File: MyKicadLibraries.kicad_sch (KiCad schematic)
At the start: 34 parts, among them J1 Conn_01x08, J10 RCJ-22, J11 DIN-5, J12 Mini-DIN-6, J13 USB_A, J2 Conn_01x08, J3 POGO Pins, J4 c8-inlet, J5 FTDI, J6 Micro_SD_Card, J7 Conn_01x04, J8 Conn_02x04_Counter_Clockwise, J9 Conn_01x04, SW1 Schurter Switch, U1 radio-receiver, U10 rdm-6300, U11 magnetic-charger, U12 adafruit-MAX98357, U13 TTL, U14 lxb18, U15 esp32-wemos-d1-mini, U16 TCRT5000, U17 opb607a, U2 TP4056, U3 LilygoSIMT7000G, U4 esp-01m, U5 relais_module, U6 ESP-01, U7 dcdc, U8 mems-mic, U9 ESP-12E

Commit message: Add OPB607a breakout
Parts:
- added J14, J15: Conn_01x02, Connector_PinHeader_2.54mm:PinHeader_1x02_P2.54mm_Vertical, symbol Connector_Generic:Conn_01x02
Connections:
- net at U17.1: now also J15.2 (Pin_2)
- net at U17.2: now also J15.1 (Pin_1)
- net at U17.3: now also J14.2 (Pin_2)
- net at U17.4: now also J14.1 (Pin_1)
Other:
- moved on the sheet: U16
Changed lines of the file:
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@@
     (stroke (width 0) (type default) (color 0 0 0 0))
   )
+  (wire (pts (xy 62.23 25.4) (xy 62.23 26.67))
+    (stroke (width 0) (type default) (color 0 0 0 0))
+  )
   (wire (pts (xy 36.83 40.64) (xy 38.1 40.64))
+    (stroke (width 0) (type default) (color 0 0 0 0))
+  )
+  (wire (pts (xy 62.23 21.59) (xy 62.23 22.86))
+    (stroke (width 0) (type default) (color 0 0 0 0))
+  )
+  (wire (pts (xy 46.99 25.4) (xy 46.99 26.67))
+    (stroke (width 0) (type default) (color 0 0 0 0))
+  )
+  (wire (pts (xy 46.99 21.59) (xy 46.99 22.86))
     (stroke (width 0) (type default) (color 0 0 0 0))
   )
@@
     (pin "1")
   )
-  (symbol (lib_id "tcrt5000:TCRT5000") (at 30.226 24.384 0) (unit 1)
-    (in_bom yes) (on_board yes) (fields_autoplaced)
-    (property "Reference" "U16" (id 0) (at 30.226 15.24 0))
-    (property "Value" "TCRT5000" (id 1) (at 30.226 17.78 0))
-    (property "Footprint" "tcrt5000:tcrt5000" (id 2) (at 30.226 32.639 0)
-      (effects (font (size 1.27 1.27)) hide)
-    )
-    (property "Datasheet" "https://www.vishay.com/docs/83760/tcrt5000.pdf" (id 3) (at 28.956 34.544 0)
+  (symbol (lib_id "tcrt5000:TCRT5000") (at 26.416 23.876 0) (unit 1)
+    (in_bom yes) (on_board yes) (fields_autoplaced)
+    (property "Reference" "U16" (id 0) (at 26.416 14.732 0))
+    (property "Value" "TCRT5000" (id 1) (at 26.416 17.272 0))
+    (property "Footprint" "tcrt5000:tcrt5000" (id 2) (at 26.416 32.131 0)
+      (effects (font (size 1.27 1.27)) hide)
+    )
+    (property "Datasheet" "https://www.vishay.com/docs/83760/tcrt5000.pdf" (id 3) (at 25.146 34.036 0)
       (effects (font (size 1.27 1.27)) hide)
     )
@@
     (pin "3")
     (pin "4")
+  )
+  (symbol (lib_id "Connector_Generic:Conn_01x02") (at 67.31 25.4 0) (mirror x) (unit 1)
+    (in_bom yes) (on_board yes) (fields_autoplaced)
+    (property "Reference" "J15" (id 0) (at 67.31 16.51 0)
+      (effects (font (size 1.27 1.27)) hide)
+    )
+    (property "Value" "Conn_01x02" (id 1) (at 67.31 19.05 0)
+      (effects (font (size 1.27 1.27)) hide)
+    )
+    (property "Footprint" "Connector_PinHeader_2.54mm:PinHeader_1x02_P2.54mm_Vertical" (id 2) (at 67.31 25.4 0)
+      (effects (font (size 1.27 1.27)) hide)
+    )
+    (property "Datasheet" "~" (id 3) (at 67.31 25.4 0)
+      (effects (font (size 1.27 1.27)) hide)
+    )
+    (pin "1")
+    (pin "2")
   )
   (symbol (lib_id "LilygoSimT7000:LilygoSIMT7000G") (at 130.175 112.395 0) (unit 1)
@@
     (pin "8")
   )
+  (symbol (lib_id "Connector_Generic:Conn_01x02") (at 41.91 25.4 180) (unit 1)
+    (in_bom yes) (on_board yes) (fields_autoplaced)
+    (property "Reference" "J14" (id 0) (at 41.91 16.51 0)
+      (effects (font (size 1.27 1.27)) hide)
+    )
+    (property "Value" "Conn_01x02" (id 1) (at 41.91 19.05 0)
+      (effects (font (size 1.27 1.27)) hide)
+    )
+    (property "Footprint" "Connector_PinHeader_2.54mm:PinHeader_1x02_P2.54mm_Vertical" (id 2) (at 41.91 25.4 0)
+      (effects (font (size 1.27 1.27)) hide)
+    )
+    (property "Datasheet" "~" (id 3) (at 41.91 25.4 0)
+      (effects (font (size 1.27 1.27)) hide)
+    )
+    (pin "1")
+    (pin "2")
+  )
   (symbol (lib_id "ESP8266:ESP-12E") (at 240.665 135.255 0) (unit 1)
     (in_bom yes) (on_board yes) (fields_autoplaced)
@@
       (reference "J13") (unit 1) (value "USB_A") (footprint "usb-a-pcb:usb-a-pcb")
     )
+    (path "/d3cb2992-0631-410e-b943-8ec6f42bbcc5"
+      (reference "J14") (unit 1) (value "Conn_01x02") (footprint "Connector_PinHeader_2.54mm:PinHeader_1x02_P2.54mm_Vertical")
+    )
+    (path "/ca6d4ee7-cd0f-4062-ac98-5a85fe4a2cfe"
+      (reference "J15") (unit 1) (value "Conn_01x02") (footprint "Connector_PinHeader_2.54mm:PinHeader_1x02_P2.54mm_Vertical")
+    )
     (path "/93625391-d5f1-4afc-86f7-69a3da3b5437"

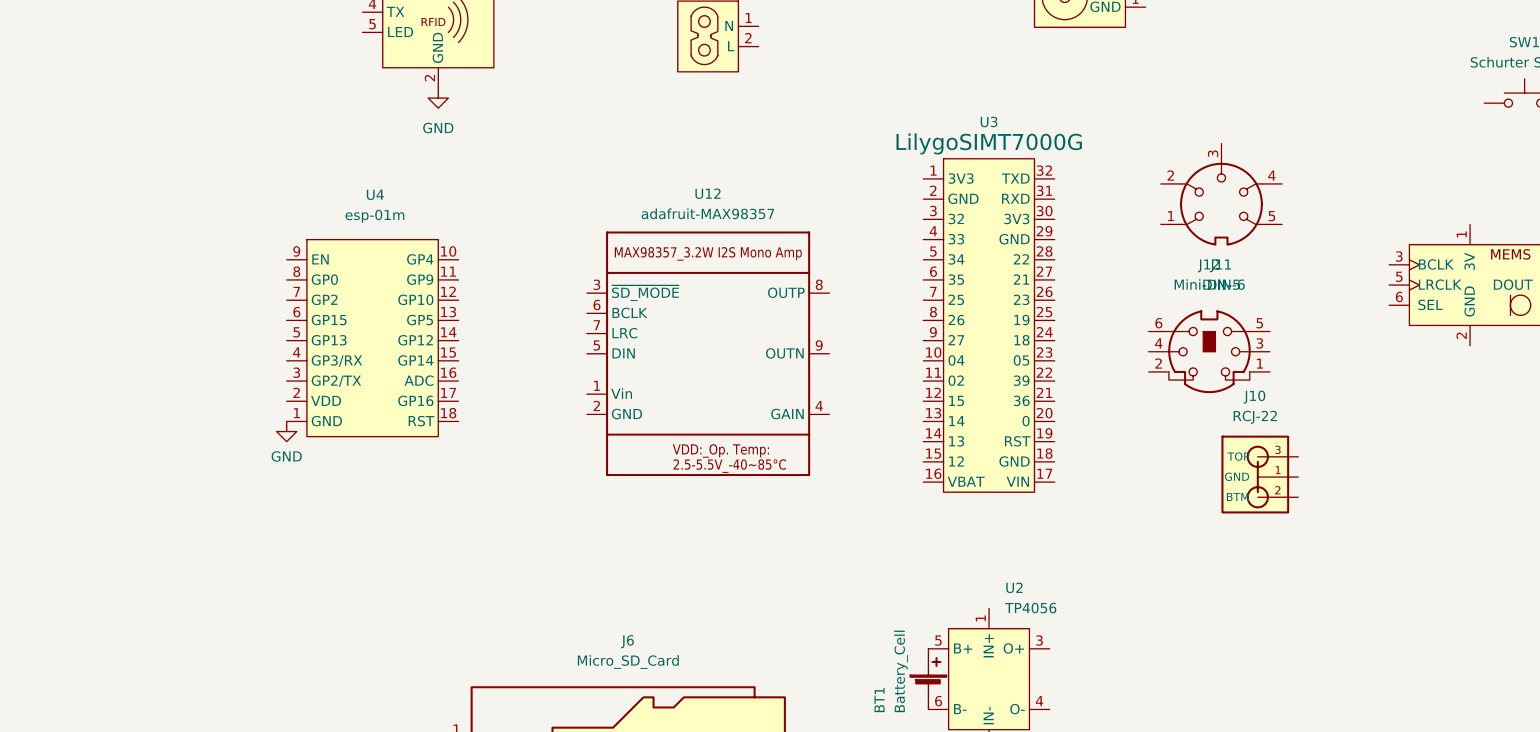
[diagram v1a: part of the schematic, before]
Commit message: Add MAX98367 footprint
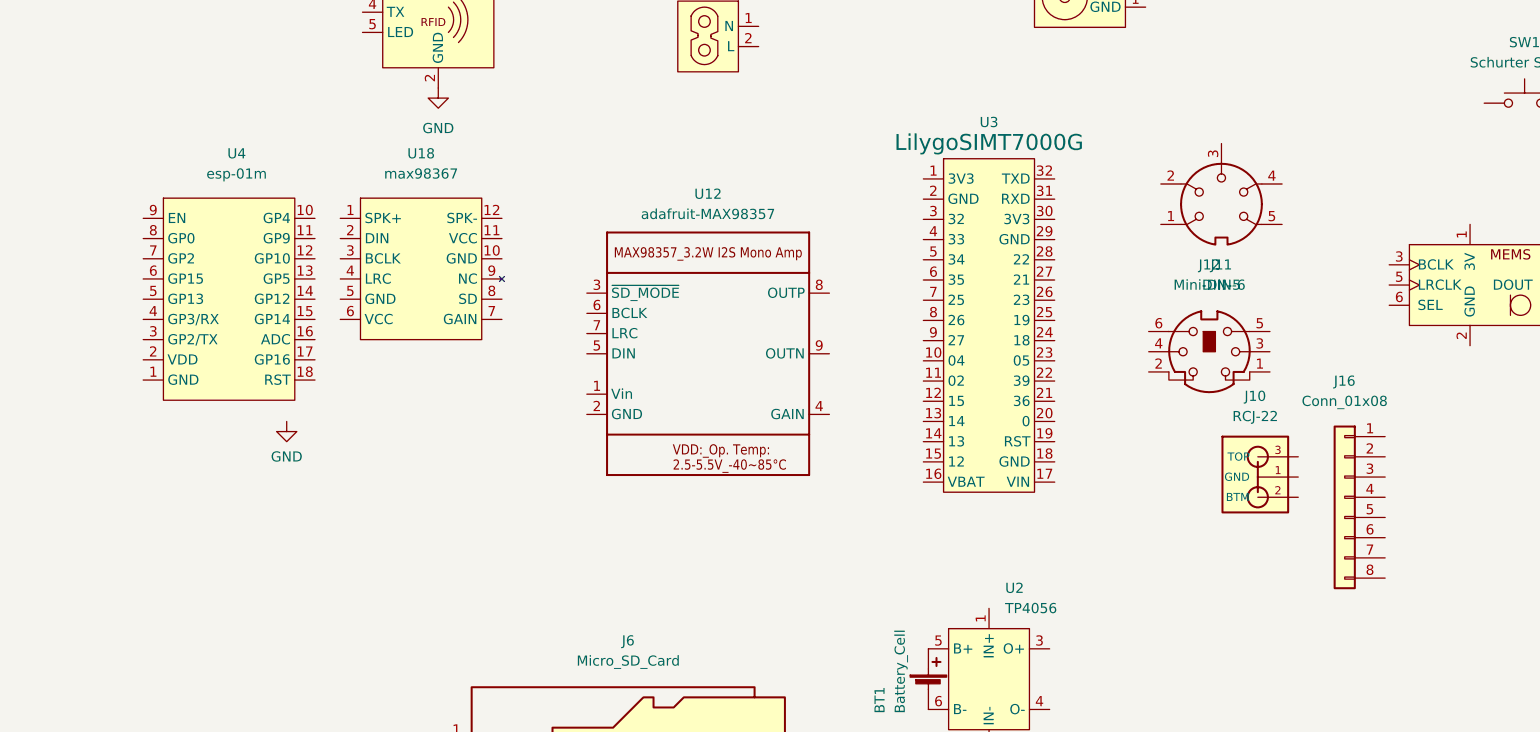
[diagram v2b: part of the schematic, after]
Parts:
- added J16: Conn_01x08, Connector_PinHeader_2.54mm:PinHeader_1x08_P2.54mm_Vertical, symbol Connector_Generic:Conn_01x08
- added U18: max98367, max98367:max98367, symbol max98367:max98367
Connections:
- net GND: no longer U4.1 (GND)
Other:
- moved on the sheet: U4
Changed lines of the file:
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@@
     (pin "6")
   )
-  (symbol (lib_id "esp-01m:esp-01m") (at 51.435 114.935 0) (unit 1)
-    (in_bom yes) (on_board yes) (fields_autoplaced)
-    (property "Reference" "U4" (id 0) (at 52.3875 96.647 0))
-    (property "Value" "esp-01m" (id 1) (at 52.3875 99.187 0))
-    (property "Footprint" "esp-01m:esp-01m" (id 2) (at 31.115 70.485 0)
-      (effects (font (size 1.27 1.27)) hide)
-    )
-    (property "Datasheet" "" (id 3) (at 31.115 70.485 0)
+  (symbol (lib_id "esp-01m:esp-01m") (at 34.036 109.728 0) (unit 1)
+    (in_bom yes) (on_board yes) (fields_autoplaced)
+    (property "Reference" "U4" (id 0) (at 34.9885 91.44 0))
+    (property "Value" "esp-01m" (id 1) (at 34.9885 93.98 0))
+    (property "Footprint" "esp-01m:esp-01m" (id 2) (at 13.716 65.278 0)
+      (effects (font (size 1.27 1.27)) hide)
+    )
+    (property "Datasheet" "https://docs.ai-thinker.com/_media/esp8266/docs/esp-01m_product_specification_en.pdf" (id 3) (at 13.716 65.278 0)
       (effects (font (size 1.27 1.27)) hide)
     )
@@
     (pin "9")
   )
+  (symbol (lib_id "Connector_Generic:Conn_01x08") (at 174.244 134.62 0) (mirror y) (unit 1)
+    (in_bom yes) (on_board yes) (fields_autoplaced)
+    (property "Reference" "J16" (id 0) (at 174.244 120.015 0))
+    (property "Value" "Conn_01x08" (id 1) (at 174.244 122.555 0))
+    (property "Footprint" "Connector_PinHeader_2.54mm:PinHeader_1x08_P2.54mm_Vertical" (id 2) (at 174.244 134.62 0)
+      (effects (font (size 1.27 1.27)) hide)
+    )
+    (property "Datasheet" "~" (id 3) (at 174.244 134.62 0)
+      (effects (font (size 1.27 1.27)) hide)
+    )
+    (pin "1")
+    (pin "2")
+    (pin "3")
+    (pin "4")
+    (pin "5")
+    (pin "6")
+    (pin "7")
+    (pin "8")
+  )
+  (symbol (lib_id "max98367:max98367") (at 58.166 105.918 0) (unit 1)
+    (in_bom yes) (on_board yes) (fields_autoplaced)
+    (property "Reference" "U18" (id 0) (at 58.166 91.44 0))
+    (property "Value" "max98367" (id 1) (at 58.166 93.98 0))
+    (property "Footprint" "max98367:max98367" (id 2) (at 58.801 97.028 0)
+      (effects (font (size 1.27 1.27)) hide)
+    )
+    (property "Datasheet" "https://www.dfrobot.com/product-2614.html" (id 3) (at 58.801 97.028 0)
+      (effects (font (size 1.27 1.27)) hide)
+    )
+    (pin "1")
+    (pin "10")
+    (pin "11")
+    (pin "12")
+    (pin "2")
+    (pin "3")
+    (pin "4")
+    (pin "5")
+    (pin "6")
+    (pin "7")
+    (pin "8")
+    (pin "9")
+  )
   (symbol (lib_id "Connector_Generic:Conn_02x04_Counter_Clockwise") (at 247.904 26.67 0) (unit 1)
     (in_bom yes) (on_board yes) (fields_autoplaced)
@@
       (reference "J15") (unit 1) (value "Conn_01x02") (footprint "Connector_PinHeader_2.54mm:PinHeader_1x02_P2.54mm_Vertical")
     )
+    (path "/cdfe1ecd-6f59-424a-8f01-a345f2473e95"
+      (reference "J16") (unit 1) (value "Conn_01x08") (footprint "Connector_PinHeader_2.54mm:PinHeader_1x08_P2.54mm_Vertical")
+    )
     (path "/93625391-d5f1-4afc-86f7-69a3da3b5437"
       (reference "LIN1") (unit 1) (value "LEDs_In") (footprint "neopixel-strip:neopixel-strip")
@@
       (reference "U17") (unit 1) (value "opb607a") (footprint "opb607a:opb607a")
     )
-  )
+    (path "/d1953958-399d-4805-ac09-a2216d80be0a"
+      (reference "U18") (unit 1) (value "max98367") (footprint "max98367:max98367")
+    )
+  )

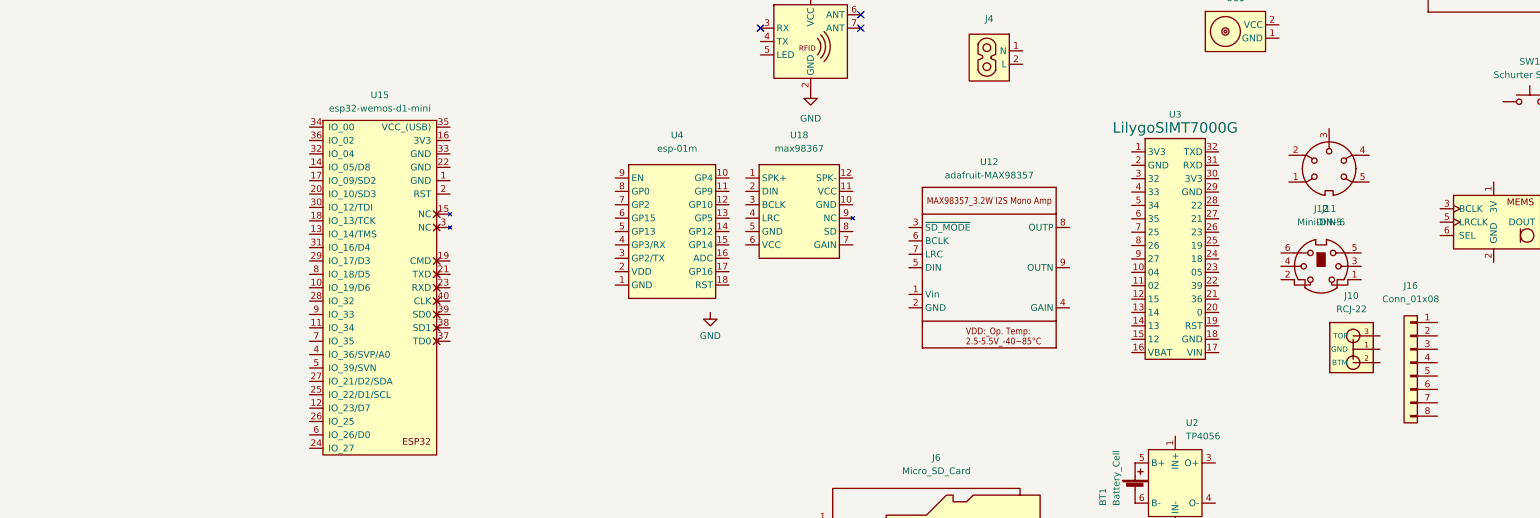
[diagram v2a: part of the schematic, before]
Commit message: Add ESP-01F footprint
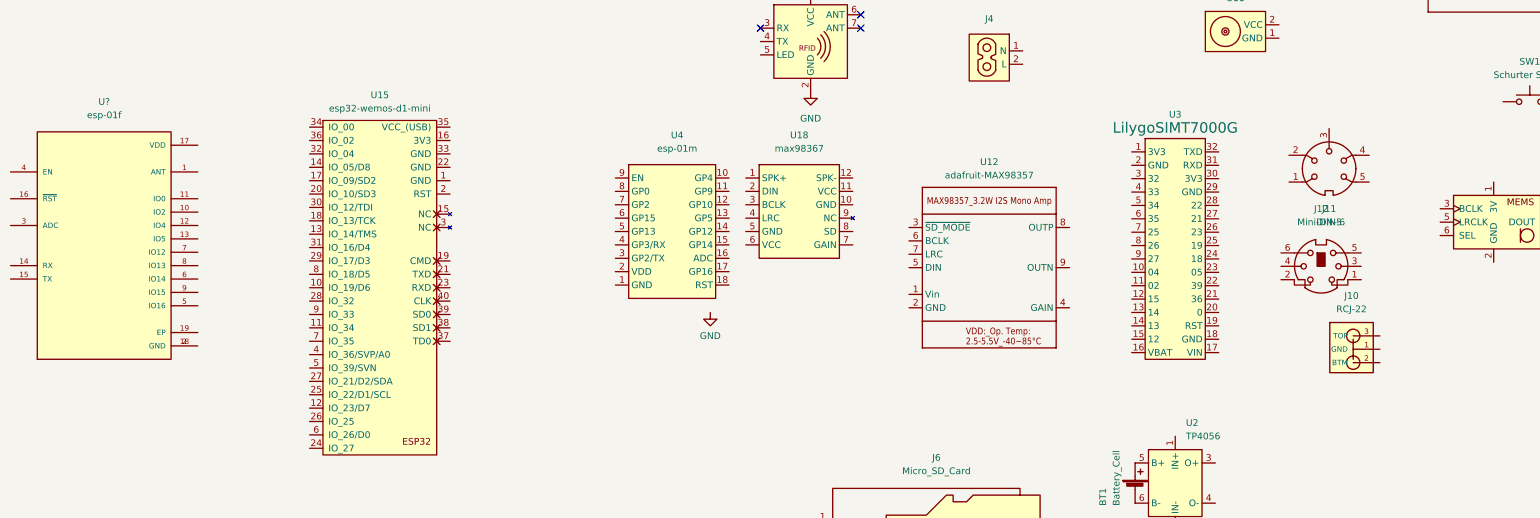
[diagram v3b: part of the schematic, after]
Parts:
- removed J16: Conn_01x08, Connector_PinHeader_2.54mm:PinHeader_1x08_P2.54mm_Vertical, symbol Connector_Generic:Conn_01x08
- added U?: esp-01f, esp-01f:esp-01f, symbol esp-01F:esp-01f
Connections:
- new net: U?.18 (GND), U?.2 (GND)

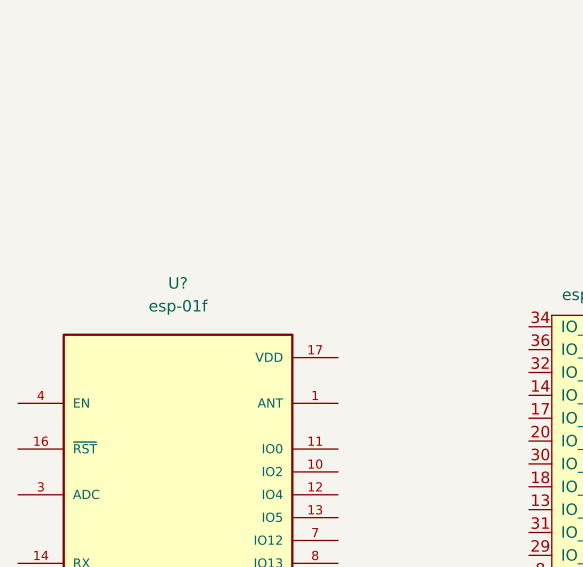
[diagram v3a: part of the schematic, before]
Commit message: Update ESP-01F module
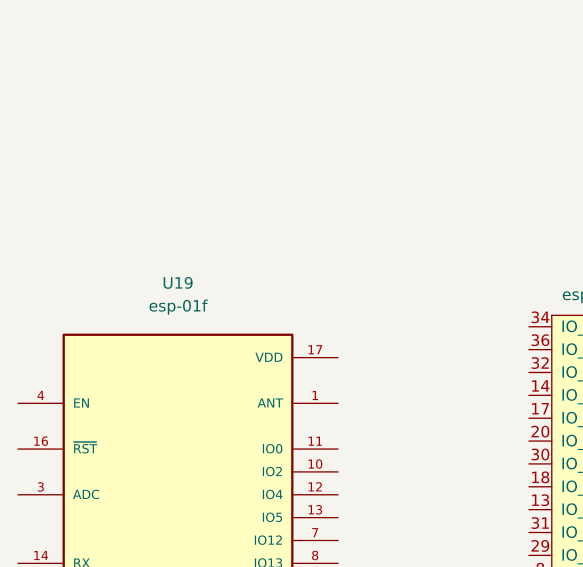
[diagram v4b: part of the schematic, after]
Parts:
- gave numbers to parts that had none: 1
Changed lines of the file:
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@@
   (symbol (lib_id "esp-01F:esp-01f") (at -73.787 111.125 0) (unit 1)
     (in_bom yes) (on_board yes) (fields_autoplaced)
-    (property "Reference" "U?" (id 0) (at -73.787 85.09 0))
+    (property "Reference" "U19" (id 0) (at -73.787 85.09 0))
     (property "Value" "esp-01f" (id 1) (at -73.787 87.63 0))
     (property "Footprint" "esp-01f:esp-01f" (id 2) (at -87.122 142.875 0)
@@
     )
     (path "/a59c9e31-3e0a-452d-94a1-3fdadb80282b"
-      (reference "U?") (unit 1) (value "esp-01f") (footprint "esp-01f:esp-01f")
-    )
-  )
+      (reference "U19") (unit 1) (value "esp-01f") (footprint "esp-01f:esp-01f")
+    )
+  )

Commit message: Update ESP01m library
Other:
- title: (none) -> My Kicad Libraries
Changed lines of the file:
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@@
 (kicad_sch (version 20211123) (generator eeschema)
   (paper "A4")
+  (title_block
+    (title "My Kicad Libraries")
+    (date "2023-12-23")
+  )
   (no_connect (at 50.8 71.12))
   (no_connect (at 69.85 68.58))
